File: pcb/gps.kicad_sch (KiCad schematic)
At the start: 2 parts, among them U3 SW_Push

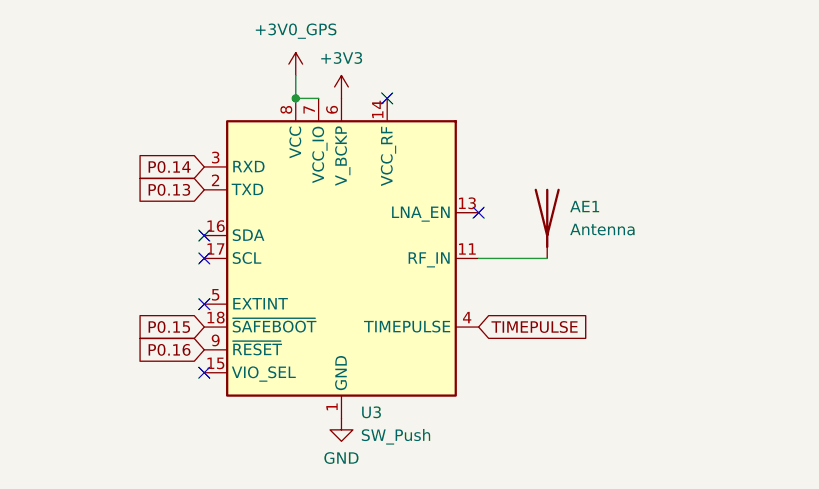
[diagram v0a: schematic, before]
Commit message: fix symbols getting absolutely goofed up
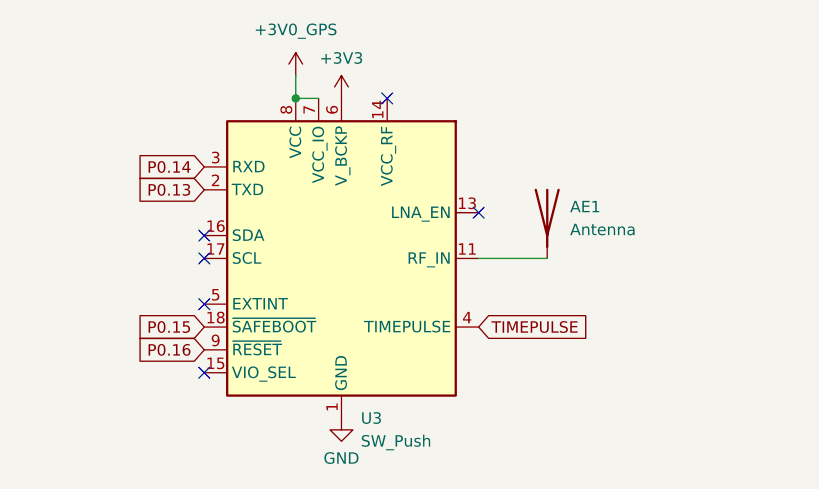
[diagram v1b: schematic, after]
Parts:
- U3: footprint (none) -> RF_GPS:ublox_MAX
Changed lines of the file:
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@@
 		(fields_autoplaced yes)
 		(property "Reference" "U3"
-			(at 157.0833 118.745 0)
+			(at 157.0833 119.38 0)
 			(show_name no)
 			(do_not_autoplace no)
@@
 		)
 		(property "Value" "SW_Push"
-			(at 157.0833 121.285 0)
+			(at 157.0833 121.92 0)
 			(show_name no)
 			(do_not_autoplace no)
@@
 			)
 		)
-		(property "Footprint" ""
+		(property "Footprint" "RF_GPS:ublox_MAX"
 			(at 165.1 118.11 0)
 			(hide yes)
@@
 			)
 		)
-		(property "Datasheet" ""
+		(property "Datasheet" "https://content.u-blox.com/sites/default/files/MAX-M10S_DataSheet_UBX-20035208.pdf"
 			(at 154.94 101.6 0)
 			(hide yes)
@@
 			)
 		)
-		(property "Description" "Push button switch, generic, two pins"
+		(property "Description" "GNSS Module MAX M10, VCC 1.65V to 3.6V"
 			(at 154.94 101.6 0)
 			(hide yes)

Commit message: fix more stuffies
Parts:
- U3: value SW_Push -> MAX-M10S
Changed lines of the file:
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@@
+			)
+		)
+		(property "KLC_S3.3" ""
+			(at 177.8 96.52 0)
+			(hide yes)
+			(show_name no)
+			(do_not_autoplace no)
+			(effects
+				(font
+					(size 1.27 1.27)
+				)
+			)
+		)
+		(property "KLC_S4.1" ""
+			(at 177.8 96.52 0)
+			(hide yes)
+			(show_name no)
+			(do_not_autoplace no)
+			(effects
+				(font
+					(size 1.27 1.27)
+				)
 			)
 		)
@@
 			)
 		)
-		(property "Value" "SW_Push"
+		(property "Value" "MAX-M10S"
 			(at 157.0833 121.92 0)
 			(show_name no)
@@
 			(at 154.94 101.6 0)
 			(hide yes)
+			(show_name no)
+			(do_not_autoplace no)
+			(effects
+				(font
+					(size 1.27 1.27)
+				)
+			)
+		)
+		(property "KLC_S3.3" ""
+			(at 154.94 101.6 0)
+			(hide yes)
+			(show_name no)
+			(do_not_autoplace no)
+			(effects
+				(font
+					(size 1.27 1.27)
+				)
+			)
+		)
+		(property "KLC_S4.1" ""
+			(at 154.94 101.6 0)
+			(hide yes)
+			(show_name no)
+			(do_not_autoplace no)
+			(effects
+				(font
+					(size 1.27 1.27)
+				)
+			)
+		)
+		(property "LCSC Part" ""
+			(at 154.94 101.6 0)
+			(hide yes)

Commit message: ALMOST done with parts purgatory
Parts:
- U3: LCSC Part (none) -> C4153167
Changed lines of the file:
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@@
 			)
 		)
-		(property "LCSC Part" ""
+		(property "LCSC Part" "C4153167"
 			(at 154.94 101.6 0)
 			(hide yes)

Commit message: starting le leyout
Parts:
- added C15: 100nF, Capacitor_SMD:C_0402_1005Metric, symbol Device:C_Small
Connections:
- net +3V0_GPS: now also C15.1
- net GND: now also C15.2
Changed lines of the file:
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@@
 	(wire
 		(pts
-			(xy 149.86 83.82) (xy 152.4 83.82)
+			(xy 149.86 81.28) (xy 149.86 83.82)
 		)
 		(stroke
@@
 	(wire
 		(pts
-			(xy 149.86 81.28) (xy 149.86 83.82)
+			(xy 128.27 83.82) (xy 152.4 83.82)
 		)
 		(stroke
@@
 	)
 	(symbol
+		(lib_id "Device:C_Small")
+		(at 128.27 86.36 0)
+		(mirror y)
+		(unit 1)
+		(body_style 1)
+		(exclude_from_sim no)
+		(in_bom yes)
+		(on_board yes)
+		(in_pos_files yes)
+		(dnp no)
+		(property "Reference" "C15"
+			(at 125.73 85.09 0)
+			(show_name no)
+			(do_not_autoplace no)
+			(effects
+				(font
+					(size 1.27 1.27)
+				)
+				(justify left)
+			)
+		)
+		(property "Value" "100nF"
+			(at 125.73 87.63 0)
+			(show_name no)
+			(do_not_autoplace no)
+			(effects
+				(font
+					(size 1.27 1.27)
+				)
+				(justify left)
+			)
+		)
+		(property "Footprint" "Capacitor_SMD:C_0402_1005Metric"
+			(at 128.27 86.36 0)
+			(hide yes)
+			(show_name no)
+			(do_not_autoplace no)
+			(effects
+				(font
+					(size 1.27 1.27)
+				)
+			)
+		)
+		(property "Datasheet" ""
+			(at 128.27 86.36 0)
+			(hide yes)
+			(show_name no)
+			(do_not_autoplace no)
+			(effects
+				(font
+					(size 1.27 1.27)
+				)
+			)
+		)
+		(property "Description" "Unpolarized capacitor, small symbol"
+			(at 128.27 86.36 0)
+			(hide yes)
+			(show_name no)
+			(do_not_autoplace no)
+			(effects
+				(font
+					(size 1.27 1.27)
+				)
+			)
+		)
+		(property "LCSC Part" "C1525"
+			(at 128.27 86.36 0)
+			(hide yes)
+			(show_name no)
+			(do_not_autoplace no)
+			(effects
+				(font
+					(size 1.27 1.27)
+				)
+			)
+		)
+		(property "KLC_S3.3" ""
+			(at 128.27 86.36 0)
+			(hide yes)
+			(show_name no)
+			(do_not_autoplace no)
+			(effects
+				(font
+					(size 1.27 1.27)
+				)
+			)
+		)
+		(property "KLC_S4.1" ""
+			(at 128.27 86.36 0)
+			(hide yes)
+			(show_name no)
+			(do_not_autoplace no)
+			(effects
+				(font
+					(size 1.27 1.27)
+				)
+			)
+		)
+		(property "LCSC" ""
+			(at 128.27 86.36 0)
+			(hide yes)
+			(show_name no)
+			(do_not_autoplace no)
+			(effects
+				(font
+					(size 1.27 1.27)
+				)
+			)
+		)
+		(property "Manufacturer Part" ""
+			(at 128.27 86.36 0)
+			(hide yes)
+			(show_name no)
+			(do_not_autoplace no)
+			(effects
+				(font
+					(size 1.27 1.27)
+				)
+			)
+		)
+		(pin "1"
+		)
+		(pin "2"
+		)
+		(instances
+			(project "watch"
+				(path "/904dae25-c5cf-4dab-9024-26ce0dbc2dd1"
+					(reference "C15")
+					(unit 1)
+				)
+			)
+		)
+	)
+	(symbol
 		(lib_id "RF_GPS:MAX-M10S")
 		(at 154.94 101.6 0)
@@
 					(unit 1)
 				)
+			)
+		)
+	)
+	(symbol
+		(lib_id "power:GND")
+		(at 128.27 88.9 0)
+		(mirror y)
+		(unit 1)
+		(body_style 1)
+		(exclude_from_sim no)
+		(in_bom yes)
+		(on_board yes)
+		(in_pos_files yes)
+		(dnp no)
+		(fields_autoplaced yes)
+		(property "Reference" "#PWR066"
+			(at 128.27 95.25 0)
+			(hide yes)
+			(show_name no)
+			(do_not_autoplace no)
+			(effects
+				(font
+					(size 1.27 1.27)
+				)
+			)
+		)
+		(property "Value" "GND"
+			(at 128.27 93.98 0)
+			(show_name no)
+			(do_not_autoplace no)
+			(effects
+				(font
+					(size 1.27 1.27)
+				)
+			)
+		)
+		(property "Footprint" ""
+			(at 128.27 88.9 0)
+			(hide yes)
+			(show_name no)
+			(do_not_autoplace no)
+			(effects
+				(font
+					(size 1.27 1.27)
+				)
+			)
+		)
+		(property "Datasheet" ""
+			(at 128.27 88.9 0)
+			(hide yes)
+			(show_name no)
+			(do_not_autoplace no)
+			(effects
+				(font
+					(size 1.27 1.27)
+				)
+			)
+		)
+		(property "Description" "Power symbol creates a global label with name \"GND\" , ground"
+			(at 128.27 88.9 0)
+			(hide yes)
+			(show_name no)
+			(do_not_autoplace no)
+			(effects
+				(font
+					(size 1.27 1.27)
+				)
+			)
+		)
+		(pin "1"
+		)
+		(instances
+			(project "watch"
+				(path "/904dae25-c5cf-4dab-9024-26ce0dbc2dd1"
+					(reference "#PWR066")
+					(unit 1)
+				)

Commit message: mogus
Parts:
- removed AE1: Antenna, JLCImport:KH-GPS181804-WY, symbol Device:Antenna
- added E1: DSGP.1575.18.4.A.02, antrenna:XCVR_DSGP.1575.18.4.A.02, symbol antenna:DSGP.1575.18.4.A.02
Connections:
- net at U3.11 (RF_IN): now also E1.1
- net P0.13 renamed P0.08
- net P0.14 renamed P0.12
- net P0.15 renamed P0.06
- net P0.16 renamed P0.11

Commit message: almost done?
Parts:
- added C16, C29: ?, symbol Device:C_Small
- added L5: ?, Inductor_SMD:L_0603_1608Metric_Pad1.05x0.95mm_HandSolder, symbol Device:L_Small
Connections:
- new net: C16.1, L5.1
- new net: C29.1, L5.2
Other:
- moved on the sheet: E1
